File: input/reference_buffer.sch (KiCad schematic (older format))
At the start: 23 parts, among them Q1 NSS1C300ET4G, U3 OPA2210

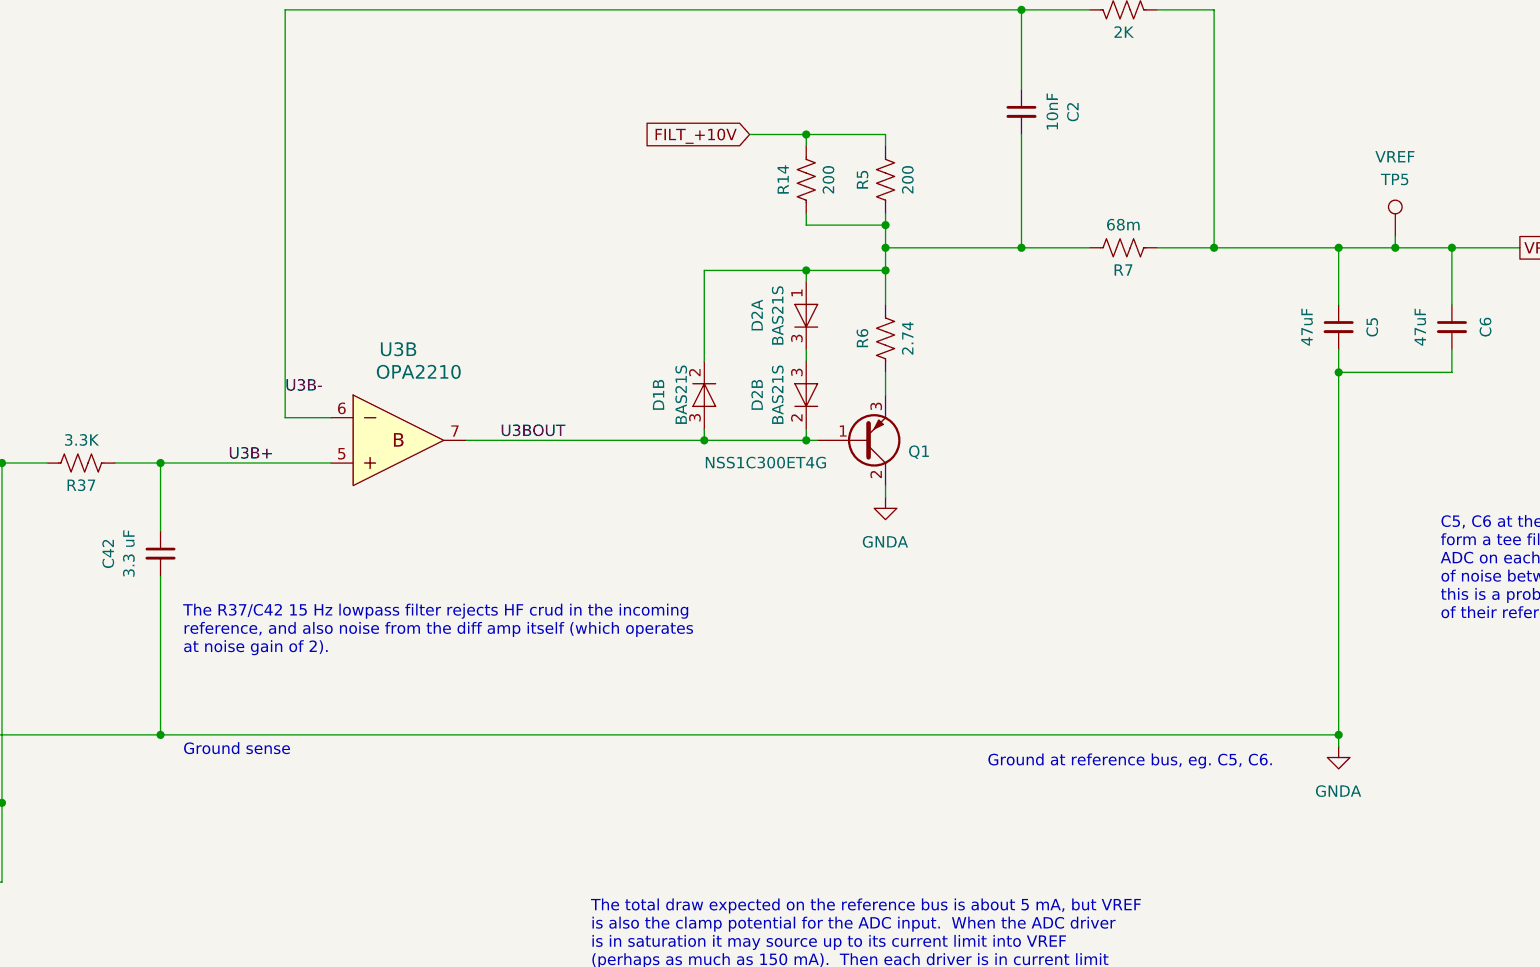
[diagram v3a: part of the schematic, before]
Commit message: ~CARDSEL and config memory added to input board schematic, but not yet to the PCB.  ~CARDSEL is now active low (before it was unimplemented).
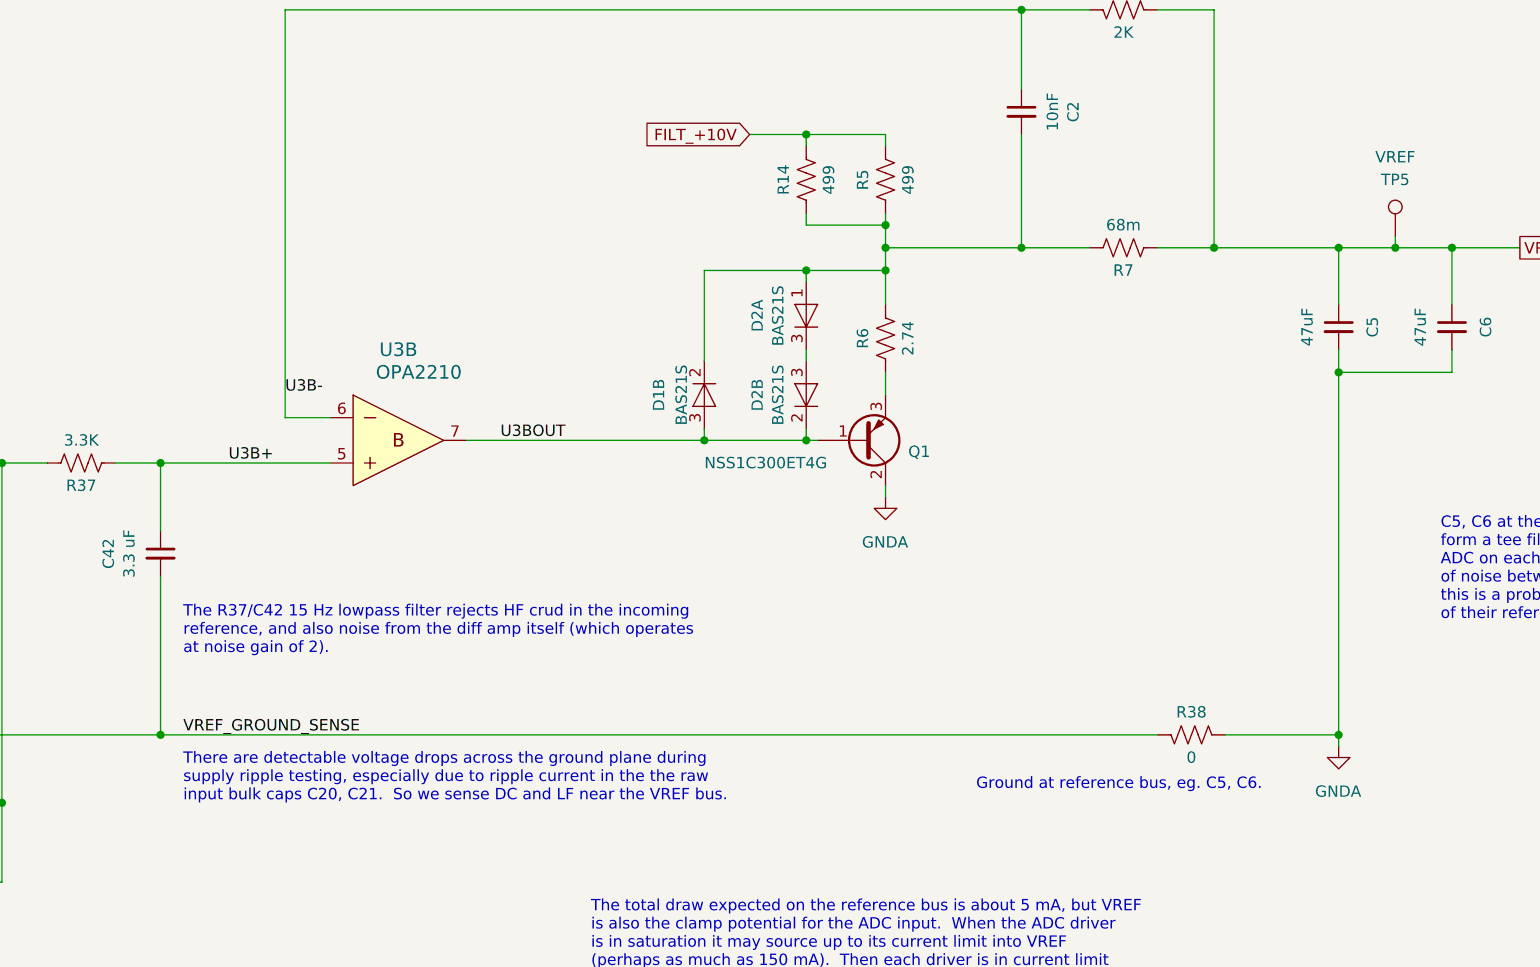
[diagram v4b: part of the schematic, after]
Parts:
- added R38: 0, Resistor_SMD:R_0603_1608Metric, symbol Device:R_US
- R14, R5: value 200 -> 499; footprint Resistor_SMD:R_0603_1608Metric -> Resistor_SMD:R_0805_2012Metric; DK line 55 -> 30; Description 200 Ohms ±1% 0.125W, 1/8W Chip Resistor 0603 (1608 Metric) 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 -> RES SMD 499 OHM 0.1% 1/4W 0805; Digikey RNCP0603FTD200RCT-ND -> A110514CT-ND; MPN RNCP0603FTD200R -> 8-2176091-9; Manufacturer Stackpole Electronics Inc -> TE Connectivity Passive Product
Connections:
- net GNDA: now also R38.1; no longer C42.2, R3.2
- new net VREF_GROUND_SENSE: C42.2, R3.2, R38.2
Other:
- note added: "There are detectable voltage drops across the ground plane during\nsupply ripple testing, especially due to ripple current in the the raw \ninput bulk caps C20, C21. So we sense DC and LF near the VREF bus."
- note removed: "Ground sense"
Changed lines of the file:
@@
 $EndComp
-Wire Wire Line
-	11650 6050 11650 6000
 Wire Wire Line
 	11650 3850 11650 4100
@@
 AR Path="/5EBEDCCA/5EACDE4D" Ref="R?"  Part="1"
 F 0 "R14" V 9400 3550 50  0000 C CNN
-F 1 "200" V 9200 3550 50  0000 C CNN
-F 2 "Resistor_SMD:R_0603_1608Metric" V 9340 3540 50  0001 C CNN
-F 3 "" H 9300 3550 50  0001 C CNN
-F 4 "200 Ohms ±1% 0.125W, 1/8W Chip Resistor 0603 (1608 Metric) Anti-Sulfur, Moisture Resistant Thin Film" H 9300 3550 50  0001 C CNN "Description"
-F 5 "RNCP0603FTD200RCT-ND" H 9300 3550 50  0001 C CNN "Digikey"
+F 1 "499" V 9200 3550 50  0000 C CNN
+F 2 "Resistor_SMD:R_0805_2012Metric" V 9340 3540 50  0001 C CNN
+F 3 "http://www.vishay.com/docs/28758/tnpw_e3.pdf" H 9300 3550 50  0001 C CNN
+F 4 "RES SMD 499 OHM 0.1% 1/4W 0805" H 9300 3550 50  0001 C CNN "Description"
+F 5 "A110514CT-ND" H 9300 3550 50  0001 C CNN "Digikey"
 F 6 "" H 9300 3550 50  0001 C CNN "Notes"
-F 7 "55" H 9300 3550 50  0001 C CNN "DK line"
-F 8 "RNCP0603FTD200R" H 9300 3550 50  0001 C CNN "MPN"
-F 9 "Stackpole Electronics Inc" H 9300 3550 50  0001 C CNN "Manufacturer"
+F 7 "30" H 9300 3550 50  0001 C CNN "DK line"
+F 8 "8-2176091-9" H 9300 3550 50  0001 C CNN "MPN"
+F 9 "TE Connectivity Passive Product" H 9300 3550 50  0001 C CNN "Manufacturer"
 	1    9300 3550
 	-1   0    0    1
@@
 AR Path="/5EBEDCCA/5EAD4090" Ref="R?"  Part="1"
 F 0 "R5" V 9750 3550 50  0000 C CNN
-F 1 "200" V 9550 3550 50  0000 C CNN
-F 2 "Resistor_SMD:R_0603_1608Metric" V 9690 3540 50  0001 C CNN
-F 3 "" H 9650 3550 50  0001 C CNN
-F 4 "200 Ohms ±1% 0.125W, 1/8W Chip Resistor 0603 (1608 Metric) Anti-Sulfur, Moisture Resistant Thin Film" H 9650 3550 50  0001 C CNN "Description"
-F 5 "RNCP0603FTD200RCT-ND" H 9650 3550 50  0001 C CNN "Digikey"
+F 1 "499" V 9550 3550 50  0000 C CNN
+F 2 "Resistor_SMD:R_0805_2012Metric" V 9690 3540 50  0001 C CNN
+F 3 "http://www.vishay.com/docs/28758/tnpw_e3.pdf" H 9650 3550 50  0001 C CNN
+F 4 "RES SMD 499 OHM 0.1% 1/4W 0805" H 9650 3550 50  0001 C CNN "Description"
+F 5 "A110514CT-ND" H 9650 3550 50  0001 C CNN "Digikey"
 F 6 "" H 9650 3550 50  0001 C CNN "Notes"
-F 7 "55" H 9650 3550 50  0001 C CNN "DK line"
-F 8 "RNCP0603FTD200R" H 9650 3550 50  0001 C CNN "MPN"
-F 9 "Stackpole Electronics Inc" H 9650 3550 50  0001 C CNN "Manufacturer"
+F 7 "30" H 9650 3550 50  0001 C CNN "DK line"
+F 8 "8-2176091-9" H 9650 3550 50  0001 C CNN "MPN"
+F 9 "TE Connectivity Passive Product" H 9650 3550 50  0001 C CNN "Manufacturer"
 	1    9650 3550
 	-1   0    0    1
@@
 Wire Wire Line
 	6450 5100 6450 4800
-Text Notes 6550 6100 0    50   ~ 0
-Ground sense
 Wire Wire Line
 	6450 4800 7200 4800
 Connection ~ 10250 2800
 Wire Wire Line
-	6450 6000 11650 6000
-Wire Wire Line
 	6450 5300 6450 6000
-Wire Wire Line
-	11650 6000 11650 4400
 Wire Wire Line
 	4600 5250 4600 5400
@@
 Wire Wire Line
 	2850 6000 6450 6000
-Connection ~ 6450 6000
-Text Notes 10100 6150 0    50   ~ 0
+Text Notes 10050 6250 0    50   ~ 0
 Ground at reference bus, eg. C5, C6.
 Text Notes 6550 5650 0    50   ~ 0
@@
 Wire Wire Line
 	7000 4600 7200 4600
-Connection ~ 11650 6000
 Text Label 6750 4800 0    50   ~ 0
 U3B+
@@
 Text Label 7950 4700 0    50   ~ 0
 U3BOUT
+Wire Wire Line
+	11650 4400 11650 6000
+$Comp
+L Device:R_US R?
+U 1 1 5FF7F603
+P 11000 6000
+AR Path="/5DFF6C0D/5FF7F603" Ref="R?"  Part="1"
+AR Path="/5E1D6729/5E1DA2AA/5FF7F603" Ref="R?"  Part="1"
+AR Path="/5E2EB92B/5FF7F603" Ref="R38"  Part="1"
+AR Path="/5E624B3C/5E2EB92B/5FF7F603" Ref="R?"  Part="1"
+AR Path="/5EBEDCCA/5FF7F603" Ref="R?"  Part="1"
+F 0 "R38" V 11100 6000 50  0000 C CNN
+F 1 "0" V 10900 6000 50  0000 C CNN
+F 2 "Resistor_SMD:R_0603_1608Metric" V 11040 5990 50  0001 C CNN
+F 3 "?" H 11000 6000 50  0001 C CNN
+F 4 "" V 11000 6000 50  0001 C CNN "Notes"
+F 5 "" H 11000 6000 50  0001 C CNN "DK line"
+F 6 "?" H 11000 6000 50  0001 C CNN "Description"
+F 7 "" H 11000 6000 50  0001 C CNN "Digikey"
+F 8 "" H 11000 6000 50  0001 C CNN "MPN"
+F 9 "" H 11000 6000 50  0001 C CNN "Manufacturer"
+	1    11000 6000
+	0    1    -1   0
+$EndComp
+Wire Wire Line
+	10850 6000 6450 6000
+Connection ~ 6450 6000
+Wire Wire Line
+	11150 6000 11650 6000
+Connection ~ 11650 6000
+Wire Wire Line
+	11650 6000 11650 6050
+Text Label 6550 6000 0    50   ~ 0
+VREF_GROUND_SENSE
+Text Notes 6550 6300 0    50   ~ 0
+There are detectable voltage drops across the ground plane during\nsupply ripple testing, especially due to ripple current in the the raw \ninput bulk caps C20, C21.  So we sense DC and LF near the VREF bus.
 $EndSCHEMATC

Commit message: More work on in_panel.  Also, shortened input_board by 10mm and tweaked the testpoints a bit, added another GND, and changed the supply TPs to be a hookable type.
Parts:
- TP5: footprint TestPoint:TestPoint_THTPad_D1.5mm_Drill0.7mm -> TestPoint:TestPoint_Keystone_5000-5004_Miniature
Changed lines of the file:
@@
 F 0 "TP5" H 11900 4050 50  0000 C CNN
 F 1 "VREF" H 11900 4150 50  0000 C CNN
-F 2 "TestPoint:TestPoint_THTPad_D1.5mm_Drill0.7mm" H 12100 3800 50  0001 C CNN
+F 2 "TestPoint:TestPoint_Keystone_5000-5004_Miniature" H 12100 3800 50  0001 C CNN
 F 3 "~" H 12100 3800 50  0001 C CNN
 F 4 "Do Not Populate" H 11900 3800 50  0001 C CNN "Description"

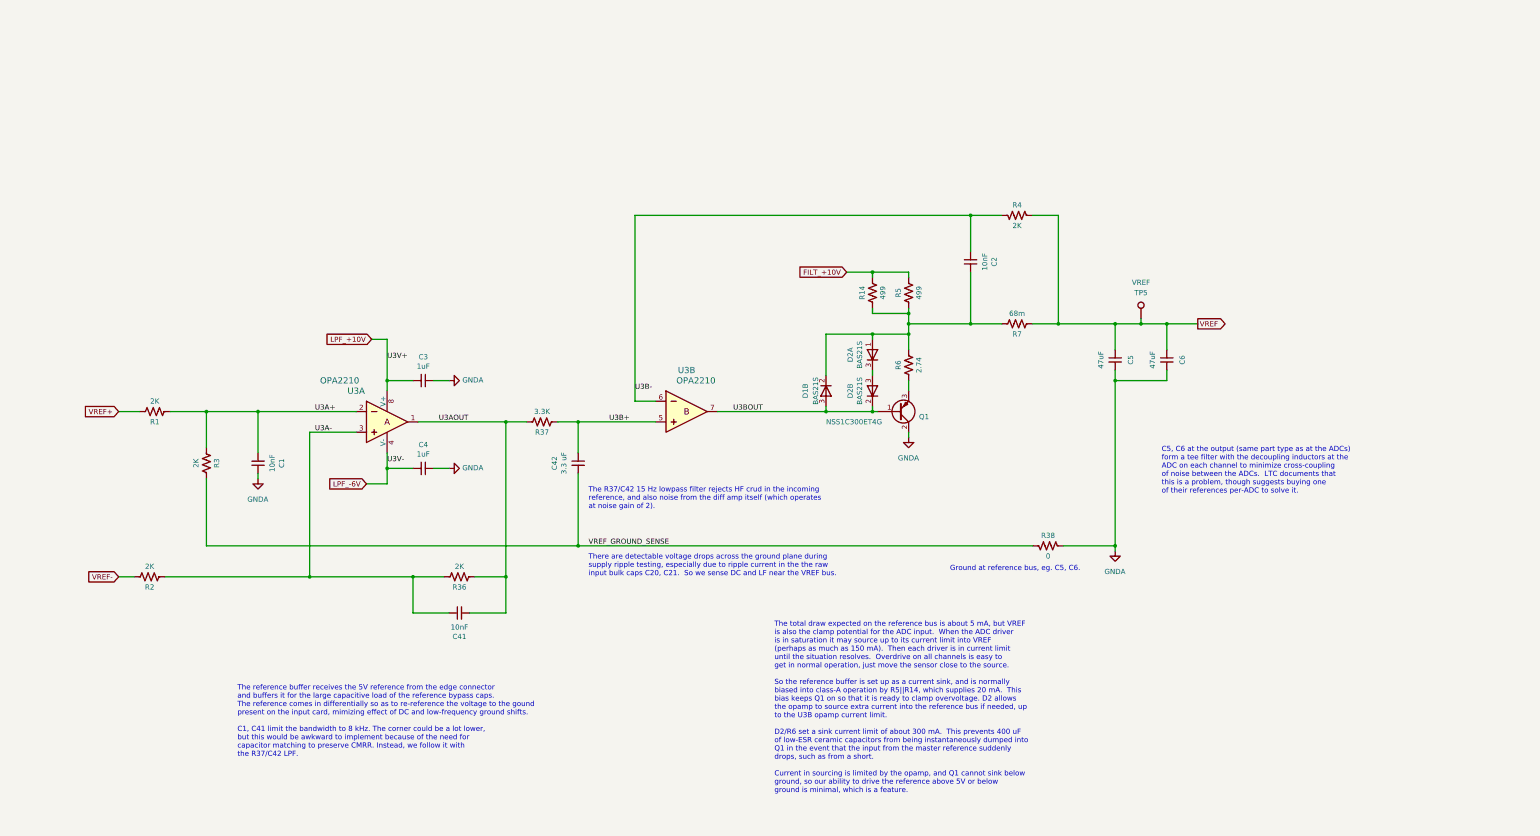
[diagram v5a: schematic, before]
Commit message: Input board revisions, mostly related to reference buffer.
power.sch: changed +3.3V to use the NCP1117 adjustable regulator, the MCP1577 was so noisy it was injecting noise into the ground plane, disturbing the VREF distribution.  Fixed fuse footprint, was too small.

reference_buffer.sch: added series resistor R40 on VREF buffer feedback cap C2, this adds damping to the response, avoiding noise peaking and overshoot.  Changed VREF bias R5/R14 to be taken from V+, rather than FILT_+10V.  V+ is a much lower noise regulated output, but this does reintroduce a bootstrapping issue between VREF and V+.  We don't get any startup problems here, though, because U3B can source current into VREF (from LPF_+10V) until the V+ supply comes up.  Because of 8V rather than 10V, the bias resistors are changed to 301 Ohm to maintain 20 mA bias. Change the VREF bus capacitor from  2x 47 uF ceramic to 330 uF aluminum poly.  This improves damping and disturbance rejection between 10 kHz and 100 kHz.

input_board.kicad_pcb: update for these schematic changes.

reference_buffer_lpf.wxsch: update to match current design.
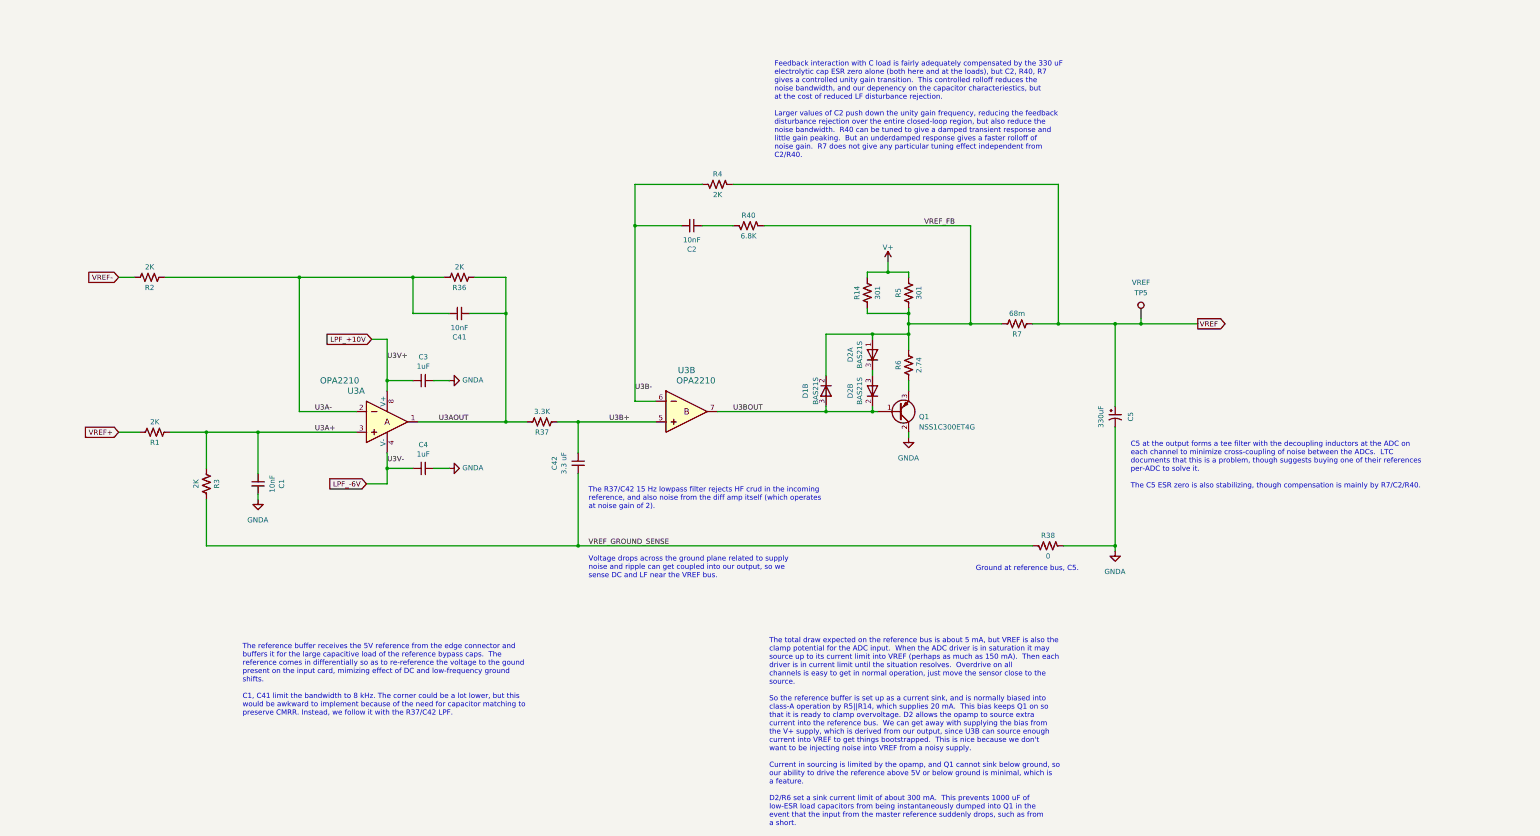
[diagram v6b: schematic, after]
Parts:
- removed C5, C6: 47uF, Capacitor_SMD:C_1210_3225Metric, symbol Device:C_Small
- added C5: 330uF, Capacitor_SMD:CP_Elec_8x6.7, symbol Device:CP1_Small
- added R40: 6.8K, Resistor_SMD:R_0603_1608Metric, symbol Device:R_US
- R14, R5: value 499 -> 301; DK line 30 -> 50; Description RES SMD 499 OHM 0.1% 1/4W 0805 -> 301 Ohms ±1% 0.125W, 1/8W Chip Resistor 0603 (1608 Metric) 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; Digikey A110514CT-ND -> RNCP0603FTD301RCT-ND; MPN 8-2176091-9 -> RNCP0603FTD301R; Manufacturer TE Connectivity Passive Product -> Stackpole Electronics Inc; Notes (none) -> 0.1%
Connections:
- net GNDA: now also C5.2
- net U3A+: now also U3.3; no longer U3.2
- net U3A-: now also U3.2; no longer U3.3
- net U3B-: now also C2.2; no longer C2.1
- net VREF: now also C5.1
- net VREF_FB: now reaches D1.1 (A), D2.2 (K), R14.1, R5.1, R5.2, R6.2
- net VREF_FB: now also R40.1; no longer C2.2
- net FILT_+10V renamed V+
- new net: C2.1, R40.2
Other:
- note added: "C5 at the output forms a tee filter with the decoupling inductors at the ADC on\neach channel to minimize cross-coupling of noise between the ADCs. LTC\ndocuments that this is a problem, though suggests buying one of their references\nper-ADC to solve it.\n\nThe C5 ESR zero is also stabilizing, though compensation is mainly by R7/C2/R40."
- note added: "Feedback interaction with C load is fairly adequately compensated by the 330 uF\nelectrolytic cap ESR zero alone (both here and at the loads), but C2, R40, R7\ngives a controlled unity gain transition. This controlled rolloff reduces the\nnoise bandwidth, and our depenency on the capacitor characteriestics, but\nat the cost of reduced LF disturbance rejection.\n\nLarger values of C2 push down the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"
- note added: "Ground at reference bus, C5."
- note added: "The reference buffer receives the 5V reference from the edge connector and\nbuffers it for the large capacitive load of the reference bypass caps. The\nreference comes in differentially so as to re-reference the voltage to the gound\npresent on the input card, mimizing effect of DC and low-frequency ground\nshifts.\n\nC1, C41 limit the bandwidth to 8 kHz. The corner could be a lot lower, but this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"
- note added: "The total draw expected on the reference bus is about 5 mA, but VREF is also the\nclamp potential for the ADC input. When the ADC driver is in saturation it may\nsource up to its current limit into VREF (perhaps as much as 150 mA). Then each\ndriver is in current limit until the situation resolves. Overdrive on all\nchannels is easy to get in normal operation, just move the sensor close to the\ns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"
- note added: "Voltage drops across the ground plane related to supply\nnoise and ripple can get coupled into our output, so we\nsense DC and LF near the VREF bus.\n\n"
- note removed: "C5, C6 at the output (same part type as at the ADCs)\nform a tee filter with the decoupling inductors at the \nADC on each channel to minimize cross-coupling\nof noise between the ADCs. LTC documents that\nthis is a problem, though suggests buying one\nof their references per-ADC to solve it."
- note removed: "Ground at reference bus, eg. C5, C6."
- note removed: "The reference buffer receives the 5V reference from the edge connector\nand buffers it for the large capacitive load of the reference bypass caps. \nThe reference comes in differentially so as to re-reference the voltage to the gound\npresent on the input card, mimizing effect of DC and low-frequency ground shifts.\n\nC1, C41 limit the bandwidth to 8 kHz. The corner could be a lot lower,\nbut thi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"
- note removed: "The total draw expected on the reference bus is about 5 mA, but VREF\nis also the clamp potential for the ADC input. When the ADC driver\nis in saturation it may source up to its current limit into VREF\n(perhaps as much as 150 mA). Then each driver is in current limit\nuntil the situation resolves. Overdrive on all channels is easy to\nget in normal operation, just move the sensor close to the s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"
- note removed: "There are detectable voltage drops across the ground plane during\nsupply ripple testing, especially due to ripple current in the the raw \ninput bulk caps C20, C21. So we sense DC and LF near the VREF bus."
- moved on the sheet: C1, C2, C41, R1, R2, R3, R36, R4
